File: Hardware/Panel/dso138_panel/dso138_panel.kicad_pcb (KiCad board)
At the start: 2 copper layers, 100 x 200 mm, 27 parts

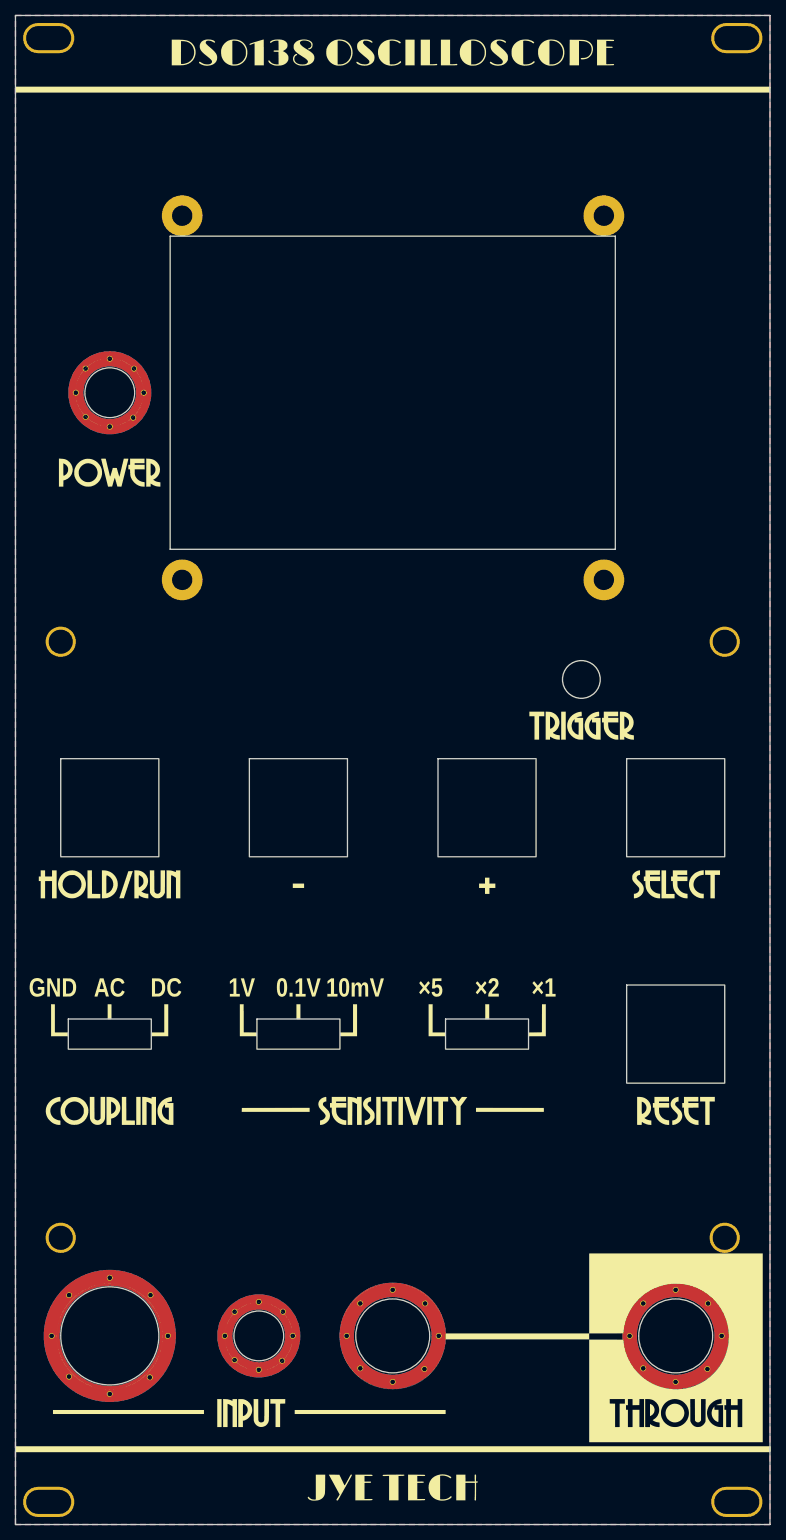
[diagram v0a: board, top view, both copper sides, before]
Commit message: TO-220 regulator; panel
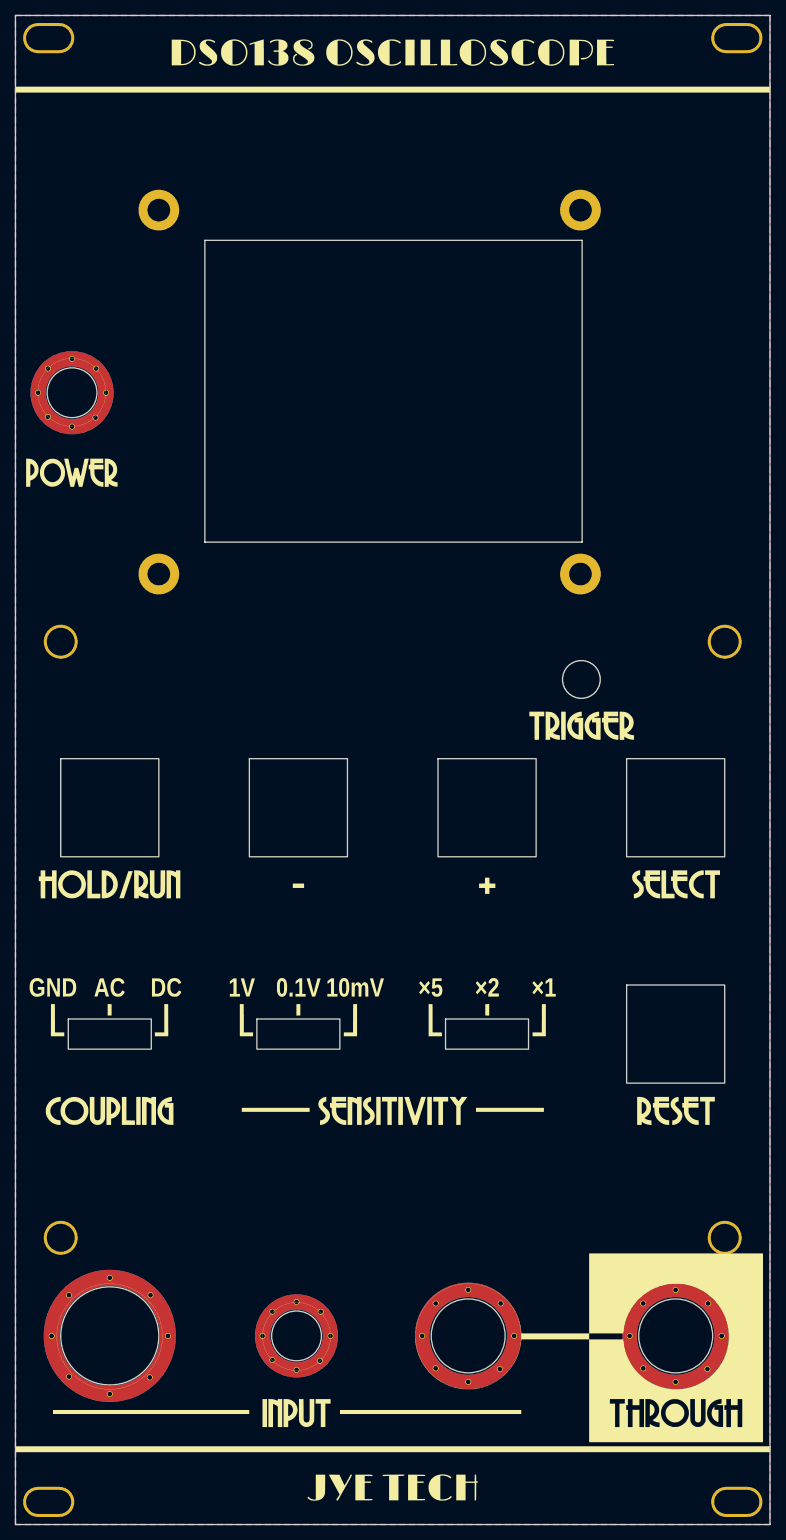
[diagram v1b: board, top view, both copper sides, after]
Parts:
- GRAF3: footprint ao_tht:CC0_logo -> AO_tht:CC0_logo
- H23, H24: footprint Kosmo_panel:Kosmo_Panel_Dual_Slotted_Mounting_Holes -> Kosmo_panel_NPTH:Kosmo_Panel_Dual_Slotted_Mounting_Holes
- moved H9 10.0 mm to (110.0, 175.0)
- moved H10 5.00 mm to (57.5, 50.0)
- moved H5 5.00 mm to (87.2, 175.0)
- moved H19 3.19 mm to (124.9, 74.0)
- moved H18 3.19 mm to (69.0, 74.0)
- moved H20 3.19 mm to (124.9, 25.8)
- moved H21 3.19 mm to (69.0, 25.8)
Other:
- outline, holes or cut-outs redrawn
- board text added: "Panel design by Rich Holmes 02/2023 CC0 1.0 JLCJLCJLCJLC"
- board text removed: "Panel design by Rich Holmes 11/2022 CC0 1.0 JLCJLCJLCJLC"

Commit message: gerbers
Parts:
- H1, H11, H15, H16, H6: footprint Kosmo_panel_NPTH:Kosmo_Tact_Button_13mm_square_Hole -> Kosmo_panel:Kosmo_Tact_Button_13mm_square_Hole
- H10, H5: footprint Kosmo_panel_NPTH:Kosmo_Switch_Hole -> Kosmo_panel:Kosmo_Switch_Hole
- H12, H2, H7: footprint Kosmo_panel_NPTH:Kosmo_DP3T_Slide_Switch_Hole -> Kosmo_panel:Kosmo_DP3T_Slide_Switch_Hole
- H13, H17, H3, H8: footprint Kosmo_panel_NPTH:Kosmo_Panel_Mounting_Hole -> Kosmo_panel:Kosmo_Panel_Mounting_Hole
- H14, H9: footprint Kosmo_panel_NPTH:Kosmo_Jack_Hole -> Kosmo_panel:Kosmo_Jack_Hole
- H22: footprint Kosmo_panel_NPTH:Kosmo_LED_Hole -> Kosmo_panel:Kosmo_LED_Hole
- H23, H24: footprint Kosmo_panel_NPTH:Kosmo_Panel_Dual_Slotted_Mounting_Holes -> Kosmo_panel:Kosmo_Panel_Dual_Slotted_Mounting_Holes
- H4: footprint Kosmo_panel_NPTH:Kosmo_Push_Button_Daier_Hole -> Kosmo_panel:Kosmo_Push_Button_Daier_Hole
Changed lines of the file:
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@@
   (net 0 "")
   (net 1 "GND")
-  (footprint "Kosmo_panel_NPTH:Kosmo_LED_Hole" (layer "F.Cu")
+  (footprint "Kosmo_panel:Kosmo_LED_Hole" (layer "F.Cu")
     (at 125 88)
     (descr "Mounting Hole 6mm")
@@
     (pad "" np_thru_hole circle (at 0 0) (size 5 5) (drill 5) (layers "F&B.Cu" "*.Mask"))
   )
-  (footprint "Kosmo_panel_NPTH:Kosmo_Panel_Mounting_Hole" (layer "F.Cu")
+  (footprint "Kosmo_panel:Kosmo_Panel_Mounting_Hole" (layer "F.Cu")
     (at 144 83)
     (descr "Mounting Hole 3.2mm, M3")
@@
       (net 1 "GND") (pinfunction "1") (pintype "input"))
   )
-  (footprint "Kosmo_panel_NPTH:Kosmo_Tact_Button_13mm_square_Hole" (layer "F.Cu")
+  (footprint "Kosmo_panel:Kosmo_Tact_Button_13mm_square_Hole" (layer "F.Cu")
     (at 62.5 105)
     (property "Sheetfile" "dso138_panel.kicad_sch")
@@
       (stroke (width 0) (type solid)) (fill solid) (layer "F.SilkS"))
   )
-  (footprint "Kosmo_panel_NPTH:Kosmo_Panel_Mounting_Hole" (layer "F.Cu")
+  (footprint "Kosmo_panel:Kosmo_Panel_Mounting_Hole" (layer "F.Cu")
     (at 56 162)
     (descr "Mounting Hole 3.2mm, M3")
@@
       (net 1 "GND") (pinfunction "1") (pintype "input"))
   )
-  (footprint "Kosmo_panel_NPTH:Kosmo_Panel_Mounting_Hole" (layer "F.Cu")
+  (footprint "Kosmo_panel:Kosmo_Panel_Mounting_Hole" (layer "F.Cu")
     (at 56 83)
     (descr "Mounting Hole 3.2mm, M3")
@@
       (net 1 "GND") (pinfunction "1") (pintype "input"))
   )
-  (footprint "Kosmo_panel_NPTH:Kosmo_Tact_Button_13mm_square_Hole" (layer "F.Cu")
+  (footprint "Kosmo_panel:Kosmo_Tact_Button_13mm_square_Hole" (layer "F.Cu")
     (at 137.5 135)
     (property "Sheetfile" "dso138_panel.kicad_sch")
@@
       (stroke (width 0.05) (type solid)) (fill none) (layer "F.CrtYd"))
   )
-  (footprint "Kosmo_panel_NPTH:Kosmo_Tact_Button_13mm_square_Hole" (layer "F.Cu")
+  (footprint "Kosmo_panel:Kosmo_Tact_Button_13mm_square_Hole" (layer "F.Cu")
     (at 137.5 105)
     (property "Sheetfile" "dso138_panel.kicad_sch")
@@
       (net 1 "GND") (pinfunction "1") (pintype "input"))
   )
-  (footprint "Kosmo_panel_NPTH:Kosmo_DP3T_Slide_Switch_Hole" (layer "F.Cu")
+  (footprint "Kosmo_panel:Kosmo_DP3T_Slide_Switch_Hole" (layer "F.Cu")
     (at 62.5 135)
     (property "Sheetfile" "dso138_panel.kicad_sch")
@@
       (net 1 "GND") (pinfunction "1") (pintype "input"))
   )
-  (footprint "Kosmo_panel_NPTH:Kosmo_Push_Button_Daier_Hole" (layer "F.Cu")
+  (footprint "Kosmo_panel:Kosmo_Push_Button_Daier_Hole" (layer "F.Cu")
     (at 62.5 175)
     (descr "Daier")
@@
       (net 1 "GND") (pintype "passive"))
   )
-  (footprint "Kosmo_panel_NPTH:Kosmo_Jack_Hole" (layer "F.Cu")
+  (footprint "Kosmo_panel:Kosmo_Jack_Hole" (layer "F.Cu")
     (at 110 175)
     (descr "Mounting Hole 6mm")
@@
       (net 1 "GND") (pinfunction "1") (pintype "input"))
   )
-  (footprint "Kosmo_panel_NPTH:Kosmo_Tact_Button_13mm_square_Hole" (layer "F.Cu")
+  (footprint "Kosmo_panel:Kosmo_Tact_Button_13mm_square_Hole" (layer "F.Cu")
     (at 112.5 105)
     (property "Sheetfile" "dso138_panel.kicad_sch")
@@
       (stroke (width 0.05) (type solid)) (fill none) (layer "F.CrtYd"))
   )
-  (footprint "Kosmo_panel_NPTH:Kosmo_Switch_Hole" (layer "F.Cu")
+  (footprint "Kosmo_panel:Kosmo_Switch_Hole" (layer "F.Cu")
     (at 87.25 175)
     (descr "Dailywell M1 series")
@@
       (net 1 "GND") (pintype "passive"))
   )
-  (footprint "Kosmo_panel_NPTH:Kosmo_Panel_Dual_Slotted_Mounting_Holes" (layer "F.Cu")
+  (footprint "Kosmo_panel:Kosmo_Panel_Dual_Slotted_Mounting_Holes" (layer "F.Cu")
     (at 53 197)
     (descr "Mounting Hole 3.2mm, M3")
@@
       (net 1 "GND") (pinfunction "1") (pintype "input"))
   )
-  (footprint "Kosmo_panel_NPTH:Kosmo_Jack_Hole" (layer "F.Cu")
+  (footprint "Kosmo_panel:Kosmo_Jack_Hole" (layer "F.Cu")
     (at 137.5 175)
     (descr "Mounting Hole 6mm")
@@
       (net 1 "GND") (pintype "passive") (zone_connect 2))
   )
-  (footprint "Kosmo_panel_NPTH:Kosmo_Tact_Button_13mm_square_Hole" (layer "F.Cu")
+  (footprint "Kosmo_panel:Kosmo_Tact_Button_13mm_square_Hole" (layer "F.Cu")
     (at 87.5 105)
     (property "Sheetfile" "dso138_panel.kicad_sch")
@@
       (stroke (width 0.05) (type solid)) (fill none) (layer "F.CrtYd"))
   )
-  (footprint "Kosmo_panel_NPTH:Kosmo_Panel_Mounting_Hole" (layer "F.Cu")
+  (footprint "Kosmo_panel:Kosmo_Panel_Mounting_Hole" (layer "F.Cu")
     (at 144 162)
     (descr "Mounting Hole 3.2mm, M3")
@@
       (net 1 "GND") (pinfunction "1") (pintype "input"))
   )
-  (footprint "Kosmo_panel_NPTH:Kosmo_DP3T_Slide_Switch_Hole" (layer "F.Cu")
+  (footprint "Kosmo_panel:Kosmo_DP3T_Slide_Switch_Hole" (layer "F.Cu")
     (at 87.5 135)
     (property "Sheetfile" "dso138_panel.kicad_sch")
@@
       (stroke (width 0.05) (type solid)) (fill none) (layer "F.CrtYd"))
   )
-  (footprint "Kosmo_panel_NPTH:Kosmo_DP3T_Slide_Switch_Hole" (layer "F.Cu")
+  (footprint "Kosmo_panel:Kosmo_DP3T_Slide_Switch_Hole" (layer "F.Cu")
     (at 112.5 135)
     (property "Sheetfile" "dso138_panel.kicad_sch")
@@
       (stroke (width 0.05) (type solid)) (fill none) (layer "F.CrtYd"))
   )
-  (footprint "Kosmo_panel_NPTH:Kosmo_Panel_Dual_Slotted_Mounting_Holes" (layer "F.Cu")
+  (footprint "Kosmo_panel:Kosmo_Panel_Dual_Slotted_Mounting_Holes" (layer "F.Cu")
     (at 147 3 180)
     (descr "Mounting Hole 3.2mm, M3")
@@
       (net 1 "GND") (pintype "passive") (zone_connect 2))
   )
-  (footprint "Kosmo_panel_NPTH:Kosmo_Switch_Hole" (layer "F.Cu")
+  (footprint "Kosmo_panel:Kosmo_Switch_Hole" (layer "F.Cu")
     (at 57.5 50)
     (descr "Dailywell M1 series")
